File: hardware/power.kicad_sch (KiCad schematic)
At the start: 0 parts

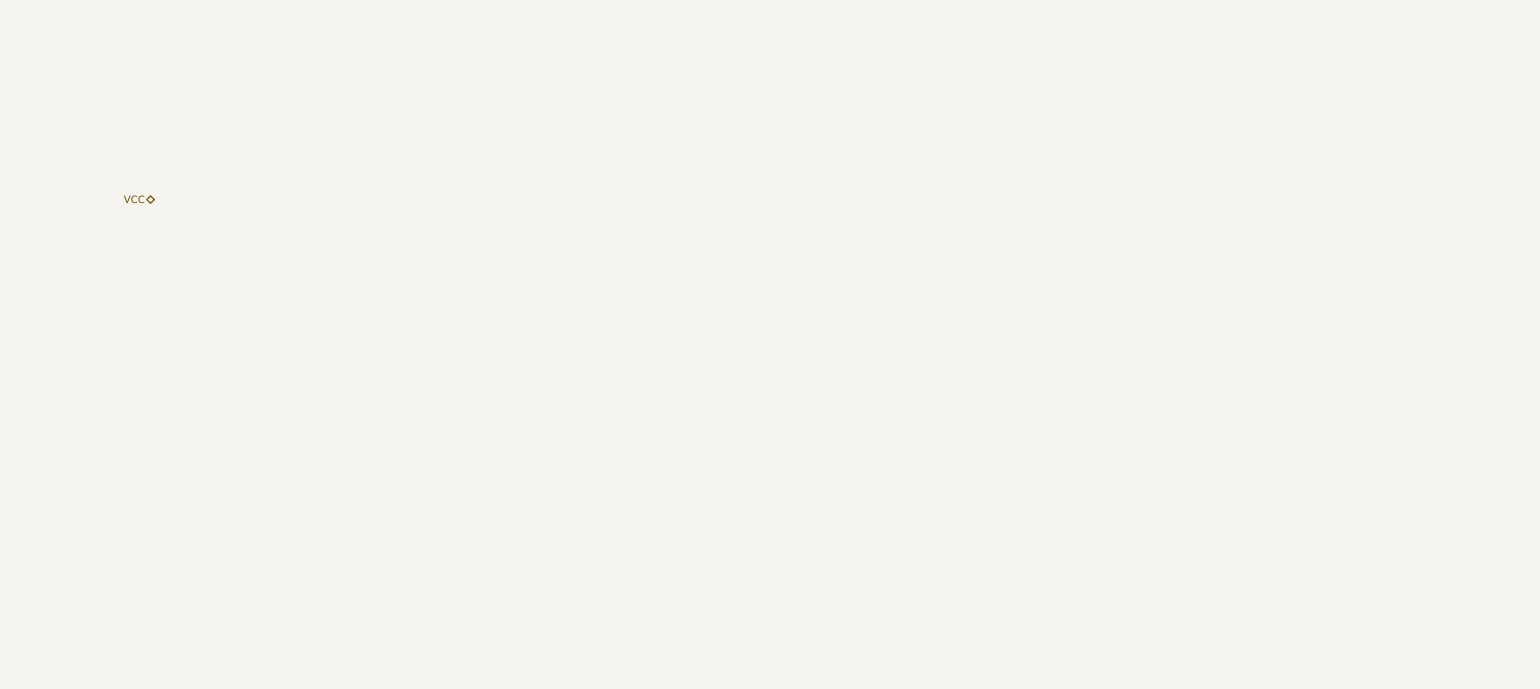
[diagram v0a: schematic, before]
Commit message: Power modules completed except 3V8
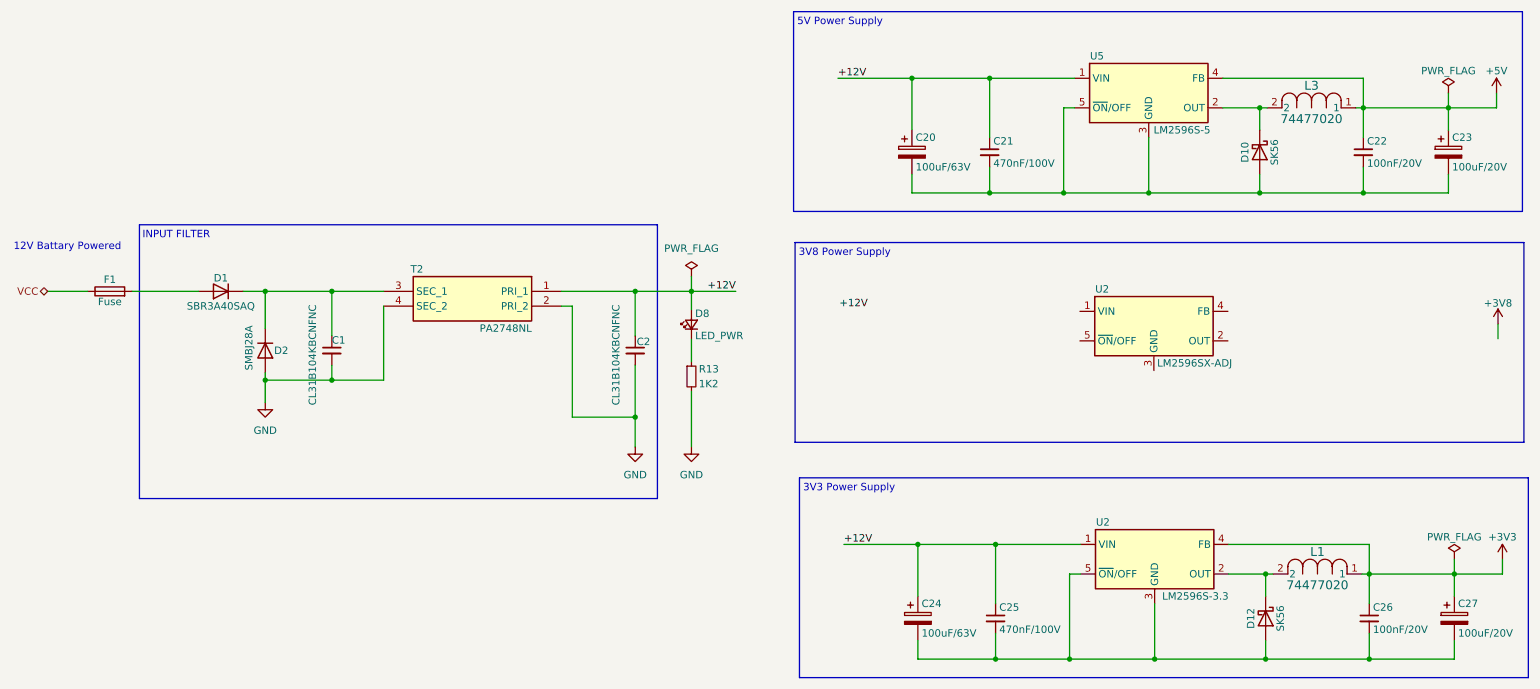
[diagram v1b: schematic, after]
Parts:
- added C1, C2: CL31B104KBCNFNC, Capacitor_SMD:C_1206_3216Metric, symbol Device:C_Small
- added C20, C24: 100uF/63V, Capacitor_SMD:CP_Elec_10x10.5, symbol Device:C_Polarized
- added C21, C25: 470nF/100V, Capacitor_SMD:C_1206_3216Metric, symbol Device:C_Small
- added C22, C26: 100nF/20V, Capacitor_SMD:C_0805_2012Metric, symbol Device:C_Small
- added C23, C27: 100uF/20V, Capacitor_SMD:CP_Elec_6.3x7.7, symbol Device:C_Polarized
- added D1: SBR3A40SAQ, Diode_SMD:D_SMA, symbol Device:D
- added D10, D12: SK56, Diode_SMD:D_SMC, symbol Device:D_Schottky
- added D2: SMBJ28A, Diode_SMD:D_SMB, symbol Device:D
- added D8: LED_PWR, LED_THT:LED_D3.0mm, symbol Device:LED_Small
- added F1: Fuse, symbol Device:Fuse
- added L1, L3: 74477020, Damlama:IND_1280-WE-PD_WRE, symbol Damlama:74477020
- added R13: 1K2, Resistor_SMD:R_0603_1608Metric, symbol Device:R_Small
- added T2: PA2748NL, Damlama:PA2748NL, symbol Damlama:PA2748NL
- added U2: LM2596S-3.3, Package_TO_SOT_SMD:TO-263-5_TabPin3, symbol Regulator_Switching:LM2596S-3.3
- added U2: LM2596SX-ADJ, Package_TO_SOT_SMD:TO-263-6, symbol Regulator_Switching:LM2596S-3.3
- added U5: LM2596S-5, Package_TO_SOT_SMD:TO-263-5_TabPin3, symbol Regulator_Switching:LM2596S-5
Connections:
- net VCC: now also F1.1
- new net: D10.1 (K), L3.2, U5.2 (OUT)
- new net: C20.2, C21.2, C22.2, C23.2, D10.2 (A), U5.3 (GND), U5.5 (~{ON}/OFF)
- new net: C1.1, D1.1 (K), D2.1 (K), T2.3 (SEC_1)
- new net: D8.1 (K), R13.1
- new net: D12.1 (K), L1.2, U2.2 (OUT)
- new net: C24.2, C25.2, C26.2, C27.2, D12.2 (A), U2.3 (GND), U2.5 (~{ON}/OFF)
- new net: D1.2 (A), F1.2
- new net +12V: C2.1, C20.1, C21.1, C24.1, C25.1, D8.2 (A), T2.1 (PRI_1), U2.1 (VIN), U5.1 (VIN)
- new net +3V3: C26.1, C27.1, L1.1, U2.4 (FB)
- new net +5V: C22.1, C23.1, L3.1, U5.4 (FB)
- new net GND: C1.2, C2.2, D2.2 (A), R13.2, T2.2 (PRI_2), T2.4 (SEC_2)
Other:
- note added: "12V Battary Powered"
- note added: "3V3 Power Supply"
- note added: "3V8 Power Supply"
- note added: "5V Power Supply"
- note added: "INPUT FILTER"
